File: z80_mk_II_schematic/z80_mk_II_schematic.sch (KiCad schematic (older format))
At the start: 0 parts

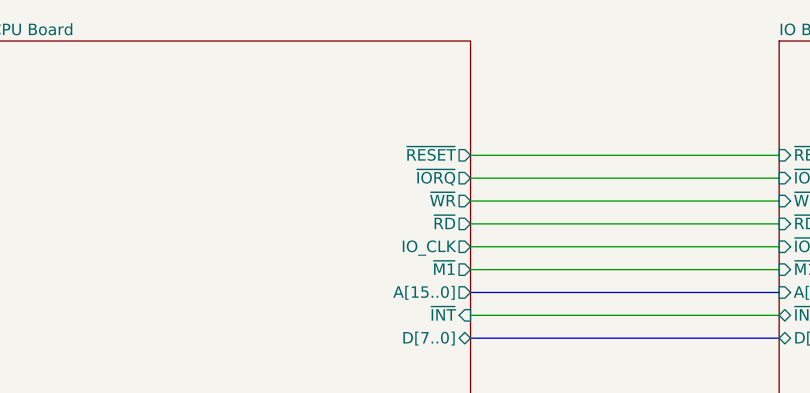
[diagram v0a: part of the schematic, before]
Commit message: Add some no-connection symbols.
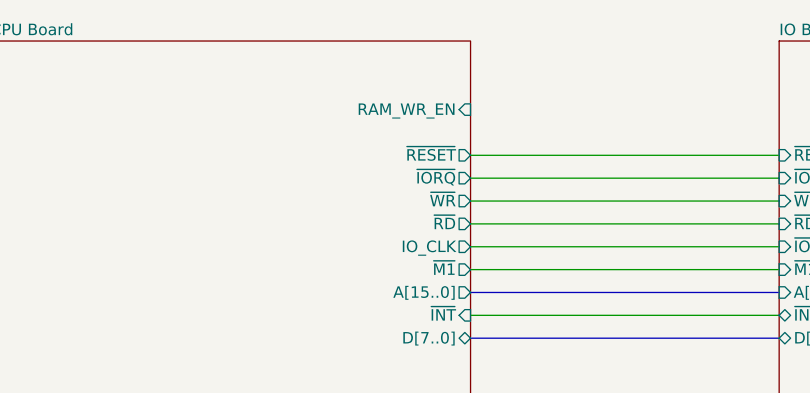
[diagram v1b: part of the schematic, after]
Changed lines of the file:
@@
 F13 "IO_CLK_IN" I L 2850 4750 50
 F14 "~EXT_RESET~" I L 2850 4850 50
+F15 "RAM_WR_EN" I R 4950 3100 50
 $EndSheet
 $Sheet

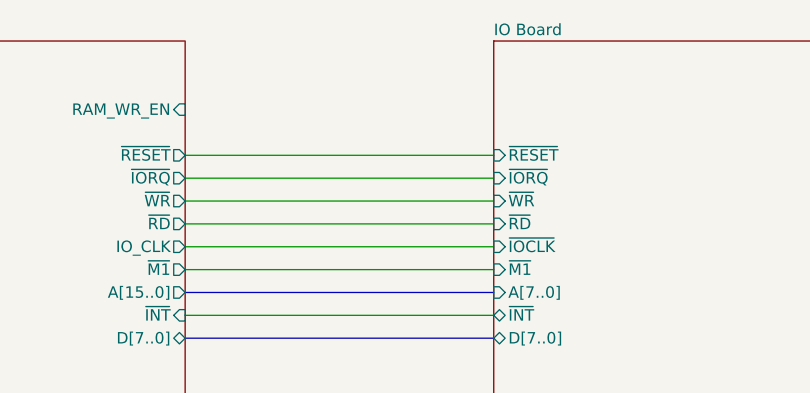
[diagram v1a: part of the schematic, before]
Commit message: Complete RAM_WR_EN wiring.
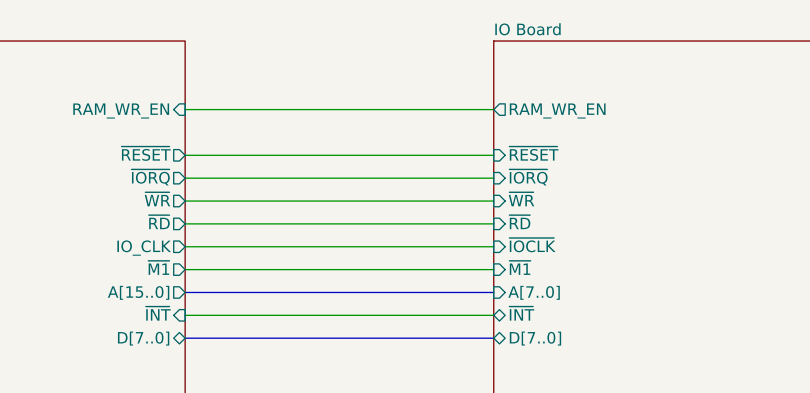
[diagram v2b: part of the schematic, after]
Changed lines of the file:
@@
 F9 "D[7..0]" B L 6300 4100 50
 F10 "~INT~" B L 6300 4000 50
+F11 "RAM_WR_EN" O L 6300 3100 50
 $EndSheet
 Wire Wire Line
@@
 Wire Wire Line
 	2500 6150 2850 6150
+Wire Wire Line
+	6300 3100 4950 3100
 $EndSCHEMATC
